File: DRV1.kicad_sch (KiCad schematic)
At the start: 15 parts

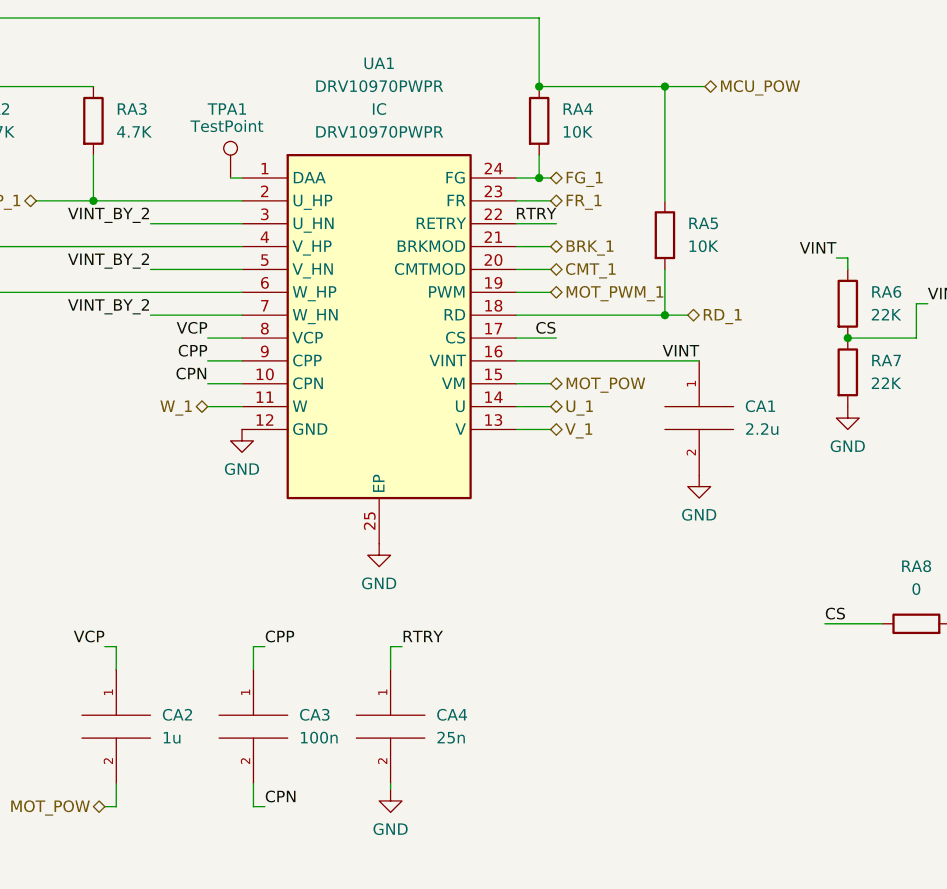
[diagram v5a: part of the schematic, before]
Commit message: Page settings changed. Added some testpoints. Some comments are made.
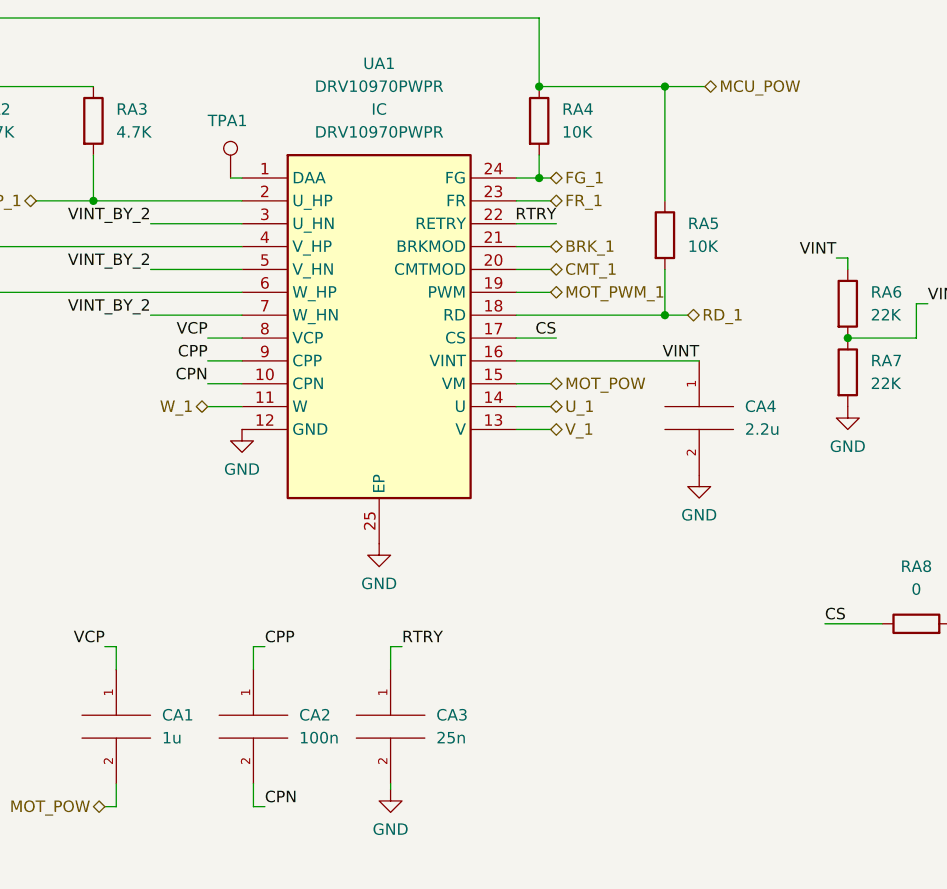
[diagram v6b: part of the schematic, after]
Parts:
- TPA1: footprint (none) -> TestPoint:TestPoint_Plated_Hole_D2.0mm
- renumbered CA2 to CA1, CA3 to CA2, CA4 to CA3, CA1 to CA4
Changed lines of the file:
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@@
   (symbol (lib_id "pspice:C") (at 124.46 147.32 0) (unit 1)
     (in_bom yes) (on_board yes) (fields_autoplaced)
-    (property "Reference" "CA2" (id 0) (at 129.54 146.0499 0)
+    (property "Reference" "CA1" (id 0) (at 129.54 146.0499 0)
       (effects (font (size 1.27 1.27)) (justify left))
     )
@@
   (symbol (lib_id "upsat-comms-hardware:GND") (at 154.94 154.305 0) (unit 1)
     (in_bom yes) (on_board yes) (fields_autoplaced)
-    (property "Reference" "#PWR014" (id 0) (at 154.94 160.655 0)
+    (property "Reference" "#PWR011" (id 0) (at 154.94 160.655 0)
       (effects (font (size 1.27 1.27)) hide)
     )
@@
   (symbol (lib_id "pspice:C") (at 139.7 147.32 0) (unit 1)
     (in_bom yes) (on_board yes) (fields_autoplaced)
-    (property "Reference" "CA3" (id 0) (at 144.78 146.0499 0)
+    (property "Reference" "CA2" (id 0) (at 144.78 146.0499 0)
       (effects (font (size 1.27 1.27)) (justify left))
     )
@@
   (symbol (lib_id "pspice:C") (at 154.94 147.32 0) (unit 1)
     (in_bom yes) (on_board yes) (fields_autoplaced)
-    (property "Reference" "CA4" (id 0) (at 160.02 146.0499 0)
+    (property "Reference" "CA3" (id 0) (at 160.02 146.0499 0)
       (effects (font (size 1.27 1.27)) (justify left))
     )
@@
   (symbol (lib_id "upsat-comms-hardware:GND") (at 138.43 114.3 0) (unit 1)
     (in_bom yes) (on_board yes) (fields_autoplaced)
-    (property "Reference" "#PWR010" (id 0) (at 138.43 120.65 0)
+    (property "Reference" "#PWR09" (id 0) (at 138.43 120.65 0)
       (effects (font (size 1.27 1.27)) hide)
     )
@@
   (symbol (lib_id "upsat-comms-hardware:GND") (at 153.67 127 0) (unit 1)
     (in_bom yes) (on_board yes) (fields_autoplaced)
-    (property "Reference" "#PWR012" (id 0) (at 153.67 133.35 0)
+    (property "Reference" "#PWR010" (id 0) (at 153.67 133.35 0)
       (effects (font (size 1.27 1.27)) hide)
     )
@@
   (symbol (lib_id "Connector:TestPoint") (at 137.16 86.36 0) (unit 1)
     (in_bom yes) (on_board yes)
-    (property "Reference" "TPA1" (id 0) (at 134.62 78.74 0)
+    (property "Reference" "TPA1" (id 0) (at 134.62 80.01 0)
       (effects (font (size 1.27 1.27)) (justify left))
     )
     (property "Value" "TestPoint" (id 1) (at 132.715 80.645 0)
-      (effects (font (size 1.27 1.27)) (justify left))
-    )
-    (property "Footprint" "" (id 2) (at 142.24 86.36 0)
+      (effects (font (size 1.27 1.27)) (justify left) hide)
+    )
+    (property "Footprint" "TestPoint:TestPoint_Plated_Hole_D2.0mm" (id 2) (at 142.24 86.36 0)
       (effects (font (size 1.27 1.27)) hide)
     )
@@
   (symbol (lib_id "upsat-comms-hardware:GND") (at 222.25 149.86 0) (unit 1)
     (in_bom yes) (on_board yes) (fields_autoplaced)
-    (property "Reference" "#PWR013" (id 0) (at 222.25 156.21 0)
+    (property "Reference" "#PWR014" (id 0) (at 222.25 156.21 0)
       (effects (font (size 1.27 1.27)) hide)
     )
@@
   (symbol (lib_id "upsat-comms-hardware:GND") (at 189.23 119.38 0) (unit 1)
     (in_bom yes) (on_board yes) (fields_autoplaced)
-    (property "Reference" "#PWR011" (id 0) (at 189.23 125.73 0)
+    (property "Reference" "#PWR012" (id 0) (at 189.23 125.73 0)
       (effects (font (size 1.27 1.27)) hide)
     )
@@
   (symbol (lib_id "pspice:C") (at 189.23 113.03 0) (unit 1)
     (in_bom yes) (on_board yes) (fields_autoplaced)
-    (property "Reference" "CA1" (id 0) (at 194.31 111.7599 0)
+    (property "Reference" "CA4" (id 0) (at 194.31 111.7599 0)
       (effects (font (size 1.27 1.27)) (justify left))
     )
@@
   (symbol (lib_id "upsat-comms-hardware:GND") (at 205.74 111.76 0) (unit 1)
     (in_bom yes) (on_board yes) (fields_autoplaced)
-    (property "Reference" "#PWR09" (id 0) (at 205.74 118.11 0)
-      (effects (font (size 1.27 1.27)) hide)
-    )
+    (property "Reference" "#PWR013" (id 0) (at 205.74 118.11 0)
+      (effects (font (size 1.27 1.27)) hide)
+    )

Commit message: I2C lines are pulled up
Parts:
- CA1, CA2, CA3, CA4: footprint (none) -> Capacitor_SMD:C_0603_1608Metric
- RA1, RA2, RA3, RA4, RA5, RA6, RA7, RA8, RA9: footprint (none) -> Resistor_SMD:R_0603_1608Metric
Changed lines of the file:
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@@
       (effects (font (size 1.27 1.27)) (justify left))
     )
-    (property "Footprint" "" (id 2) (at 124.46 147.32 0)
+    (property "Footprint" "Capacitor_SMD:C_0603_1608Metric" (id 2) (at 124.46 147.32 0)
       (effects (font (size 1.27 1.27)) hide)
     )
@@
       (effects (font (size 1.27 1.27)) (justify right))
     )
-    (property "Footprint" "" (id 2) (at 224.028 142.24 90)
+    (property "Footprint" "Resistor_SMD:R_0603_1608Metric" (id 2) (at 224.028 142.24 90)
       (effects (font (size 1.27 1.27)) hide)
     )
@@
       (effects (font (size 1.27 1.27)) (justify left))
     )
-    (property "Footprint" "" (id 2) (at 93.472 80.01 90)
+    (property "Footprint" "Resistor_SMD:R_0603_1608Metric" (id 2) (at 93.472 80.01 90)
       (effects (font (size 1.27 1.27)) hide)
     )
@@
       (effects (font (size 1.27 1.27)) (justify left))
     )
-    (property "Footprint" "" (id 2) (at 139.7 147.32 0)
+    (property "Footprint" "Capacitor_SMD:C_0603_1608Metric" (id 2) (at 139.7 147.32 0)
       (effects (font (size 1.27 1.27)) hide)
     )
@@
       (effects (font (size 1.27 1.27)) (justify left))
     )
-    (property "Footprint" "" (id 2) (at 154.94 147.32 0)
+    (property "Footprint" "Capacitor_SMD:C_0603_1608Metric" (id 2) (at 154.94 147.32 0)
       (effects (font (size 1.27 1.27)) hide)
     )
@@
       (effects (font (size 1.27 1.27)) (justify left))
     )
-    (property "Footprint" "" (id 2) (at 104.902 80.01 90)
+    (property "Footprint" "Resistor_SMD:R_0603_1608Metric" (id 2) (at 104.902 80.01 90)
       (effects (font (size 1.27 1.27)) hide)
     )
@@
     (property "Reference" "RA8" (id 0) (at 213.36 129.54 90))
     (property "Value" "0" (id 1) (at 213.36 132.08 90))
-    (property "Footprint" "" (id 2) (at 213.36 137.668 90)
+    (property "Footprint" "Resistor_SMD:R_0603_1608Metric" (id 2) (at 213.36 137.668 90)
       (effects (font (size 1.27 1.27)) hide)
     )
@@
       (effects (font (size 1.27 1.27)) (justify left))
     )
-    (property "Footprint" "" (id 2) (at 120.142 80.01 90)
+    (property "Footprint" "Resistor_SMD:R_0603_1608Metric" (id 2) (at 120.142 80.01 90)
       (effects (font (size 1.27 1.27)) hide)
     )
@@
       (effects (font (size 1.27 1.27)) (justify left))
     )
-    (property "Footprint" "" (id 2) (at 183.642 92.71 90)
+    (property "Footprint" "Resistor_SMD:R_0603_1608Metric" (id 2) (at 183.642 92.71 90)
       (effects (font (size 1.27 1.27)) hide)
     )
@@
       (effects (font (size 1.27 1.27)) (justify left))
     )
-    (property "Footprint" "" (id 2) (at 189.23 113.03 0)
+    (property "Footprint" "Capacitor_SMD:C_0603_1608Metric" (id 2) (at 189.23 113.03 0)
       (effects (font (size 1.27 1.27)) hide)
     )
@@
       (effects (font (size 1.27 1.27)) (justify left))
     )
-    (property "Footprint" "" (id 2) (at 169.672 80.01 90)
+    (property "Footprint" "Resistor_SMD:R_0603_1608Metric" (id 2) (at 169.672 80.01 90)
       (effects (font (size 1.27 1.27)) hide)
     )
@@
       (effects (font (size 1.27 1.27)) (justify left))
     )
-    (property "Footprint" "" (id 2) (at 203.962 107.95 90)
+    (property "Footprint" "Resistor_SMD:R_0603_1608Metric" (id 2) (at 203.962 107.95 90)
       (effects (font (size 1.27 1.27)) hide)
     )
@@
       (effects (font (size 1.27 1.27)) (justify left))
     )
-    (property "Footprint" "" (id 2) (at 203.962 100.33 90)
-      (effects (font (size 1.27 1.27)) hide)
-    )
+    (property "Footprint" "Resistor_SMD:R_0603_1608Metric" (id 2) (at 203.962 100.33 90)
+      (effects (font (size 1.27 1.27)) hide)
+    )

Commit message: Finalisations done, please produce BOM and fabricate
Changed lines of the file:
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@@
   )
   (text "A low-ESR ceramic capacitor must be placed in between the VM and VCP pins. TI recommends a value of 1-µF\nrated for 16 V. Place this component as close as possible to the pins."
-    (at 19.05 188.595 0)
+    (at 88.9 58.42 0)
     (effects (font (size 1.27 1.27) (thickness 0.254) bold italic) (justify left bottom))
   )
